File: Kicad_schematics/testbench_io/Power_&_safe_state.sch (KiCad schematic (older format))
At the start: 4 parts, among them J501 Conn_01x02, J502 Conn_01x02, SW501 SW_SPST, SW502 SW_SPST

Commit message: fixes
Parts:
- SW501, SW502: footprint Solar_team:RND-Slide-Switch -> Solar_team:MFP120
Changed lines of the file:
@@
 $Descr A4 11693 8268
 encoding utf-8
-Sheet 6 7
+Sheet 5 7
 Title ""
 Date ""
@@
 F 0 "SW501" H 4850 3935 50  0000 C CNN
 F 1 "SW_SPST" H 4850 3844 50  0000 C CNN
-F 2 "Solar_team:RND-Slide-Switch" H 4850 3700 50  0001 C CNN
+F 2 "Solar_team:MFP120" H 4850 3700 50  0001 C CNN
 F 3 "~" H 4850 3700 50  0001 C CNN
 	1    4850 3700
@@
 F 0 "SW502" H 6500 3685 50  0000 C CNN
 F 1 "SW_SPST" H 6500 3594 50  0000 C CNN
-F 2 "Solar_team:RND-Slide-Switch" H 6500 3450 50  0001 C CNN
+F 2 "Solar_team:MFP120" H 6500 3450 50  0001 C CNN
 F 3 "~" H 6500 3450 50  0001 C CNN
 	1    6500 3450

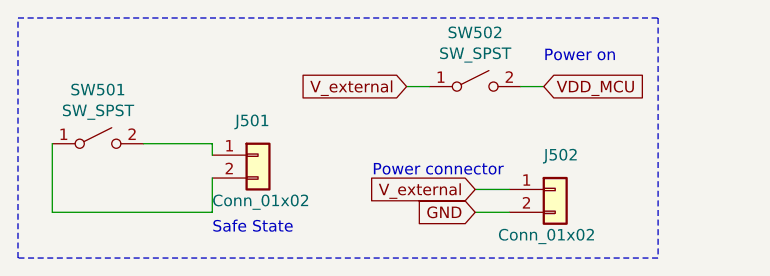
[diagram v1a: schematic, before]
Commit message: Updated CAN sheet to ethernet interface
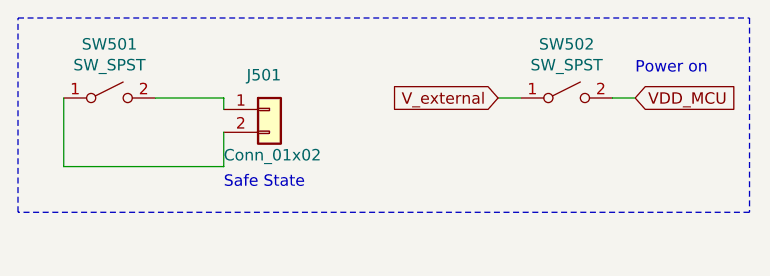
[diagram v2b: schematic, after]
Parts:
- removed J502: Conn_01x02, Connector_JST:JST_XH_S2B-XH-A_1x02_P2.50mm_Horizontal, symbol Connector_Generic:Conn_01x02
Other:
- note removed: "Power connector\n"
- moved on the sheet: J501, SW501, SW502
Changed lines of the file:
@@
 Comment4 ""
 $EndDescr
-Text Notes 6050 3850 0    50   ~ 0
-Power connector\n
-Text Notes 6800 3350 0    50   ~ 0
+Text Notes 7200 3400 0    50   ~ 0
 Power on\n
-Text Notes 5350 4100 0    50   ~ 0
+Text Notes 5400 3900 0    50   ~ 0
 Safe State\n
 Wire Notes Line
-	4500 3150 7300 3150
+	4500 3150 7700 3150
 Wire Notes Line
-	4500 4200 4500 3150
+	4500 4000 4500 3150
 Wire Notes Line
-	7300 4200 4500 4200
+	7700 4000 4500 4000
 Wire Notes Line
-	7300 3150 7300 4200
+	7700 3150 7700 4000
 Wire Wire Line
-	6650 4000 6500 4000
+	6700 3500 6600 3500
 Wire Wire Line
-	6650 3900 6500 3900
-Wire Wire Line
-	6300 3450 6200 3450
-Wire Wire Line
-	6800 3450 6700 3450
-Text GLabel 6800 3450 2    50   Input ~ 0
+	7200 3500 7100 3500
+Text GLabel 7200 3500 2    50   Input ~ 0
 VDD_MCU
-Text GLabel 6200 3450 0    50   Input ~ 0
+Text GLabel 6600 3500 0    50   Input ~ 0
 V_external
 Wire Wire Line
-	5350 3850 5350 4000
+	5400 3650 5400 3800
 Wire Wire Line
-	5350 3700 5350 3750
-Text GLabel 6500 4000 0    50   Input ~ 0
-GND
-Text GLabel 6500 3900 0    50   Input ~ 0
-V_external
-$Comp
-L Connector_Generic:Conn_01x02 J?
-U 1 1 605DE7C5
-P 6850 3900
-AR Path="/605DE7C5" Ref="J?"  Part="1"
-AR Path="/605DCA87/605DE7C5" Ref="J502"  Part="1"
-F 0 "J502" H 6800 4050 50  0000 L CNN
-F 1 "Conn_01x02" H 6600 3700 50  0000 L CNN
-F 2 "Connector_JST:JST_XH_S2B-XH-A_1x02_P2.50mm_Horizontal" H 6850 3900 50  0001 C CNN
-F 3 "~" H 6850 3900 50  0001 C CNN
-	1    6850 3900
-	1    0    0    -1
-$EndComp
+	5400 3500 5400 3550
 $Comp
 L Connector_Generic:Conn_01x02 J?
 U 1 1 605DE7CB
-P 5550 3750
+P 5600 3550
 AR Path="/605DE7CB" Ref="J?"  Part="1"
 AR Path="/605DCA87/605DE7CB" Ref="J501"  Part="1"
-F 0 "J501" H 5450 3900 50  0000 L CNN
-F 1 "Conn_01x02" H 5350 3550 50  0000 L CNN
-F 2 "Connector_JST:JST_XH_S2B-XH-A_1x02_P2.50mm_Horizontal" H 5550 3750 50  0001 C CNN
-F 3 "~" H 5550 3750 50  0001 C CNN
-	1    5550 3750
+F 0 "J501" H 5500 3700 50  0000 L CNN
+F 1 "Conn_01x02" H 5400 3350 50  0000 L CNN
+F 2 "Connector_JST:JST_XH_S2B-XH-A_1x02_P2.50mm_Horizontal" H 5600 3550 50  0001 C CNN
+F 3 "~" H 5600 3550 50  0001 C CNN
+	1    5600 3550
 	1    0    0    -1
 $EndComp
 Wire Wire Line
-	4650 4000 5350 4000
+	4700 3800 5400 3800
 Wire Wire Line
-	5350 3700 5050 3700
+	5400 3500 5100 3500
 Wire Wire Line
-	4650 3700 4650 4000
+	4700 3500 4700 3800
 $Comp
 L Switch:SW_SPST SW?
 U 1 1 605DE7D4
-P 4850 3700
+P 4900 3500
 AR Path="/605DE7D4" Ref="SW?"  Part="1"
 AR Path="/605DCA87/605DE7D4" Ref="SW501"  Part="1"
-F 0 "SW501" H 4850 3935 50  0000 C CNN
-F 1 "SW_SPST" H 4850 3844 50  0000 C CNN
-F 2 "Solar_team:MFP120" H 4850 3700 50  0001 C CNN
-F 3 "~" H 4850 3700 50  0001 C CNN
-	1    4850 3700
+F 0 "SW501" H 4900 3735 50  0000 C CNN
+F 1 "SW_SPST" H 4900 3644 50  0000 C CNN
+F 2 "Solar_team:MFP120" H 4900 3500 50  0001 C CNN
+F 3 "~" H 4900 3500 50  0001 C CNN
+	1    4900 3500
 	1    0    0    -1
 $EndComp
@@
 L Switch:SW_SPST SW?
 U 1 1 605DE7DA
-P 6500 3450
+P 6900 3500
 AR Path="/605DE7DA" Ref="SW?"  Part="1"
 AR Path="/605DCA87/605DE7DA" Ref="SW502"  Part="1"
-F 0 "SW502" H 6500 3685 50  0000 C CNN
-F 1 "SW_SPST" H 6500 3594 50  0000 C CNN
-F 2 "Solar_team:MFP120" H 6500 3450 50  0001 C CNN
-F 3 "~" H 6500 3450 50  0001 C CNN
-	1    6500 3450
+F 0 "SW502" H 6900 3735 50  0000 C CNN
+F 1 "SW_SPST" H 6900 3644 50  0000 C CNN
+F 2 "Solar_team:MFP120" H 6900 3500 50  0001 C CNN
+F 3 "~" H 6900 3500 50  0001 C CNN
+	1    6900 3500
 	1    0    0    -1
 $EndComp
